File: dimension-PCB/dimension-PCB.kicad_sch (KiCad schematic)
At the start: 260 parts, among them U1 Pico, U2 Elite-Pi

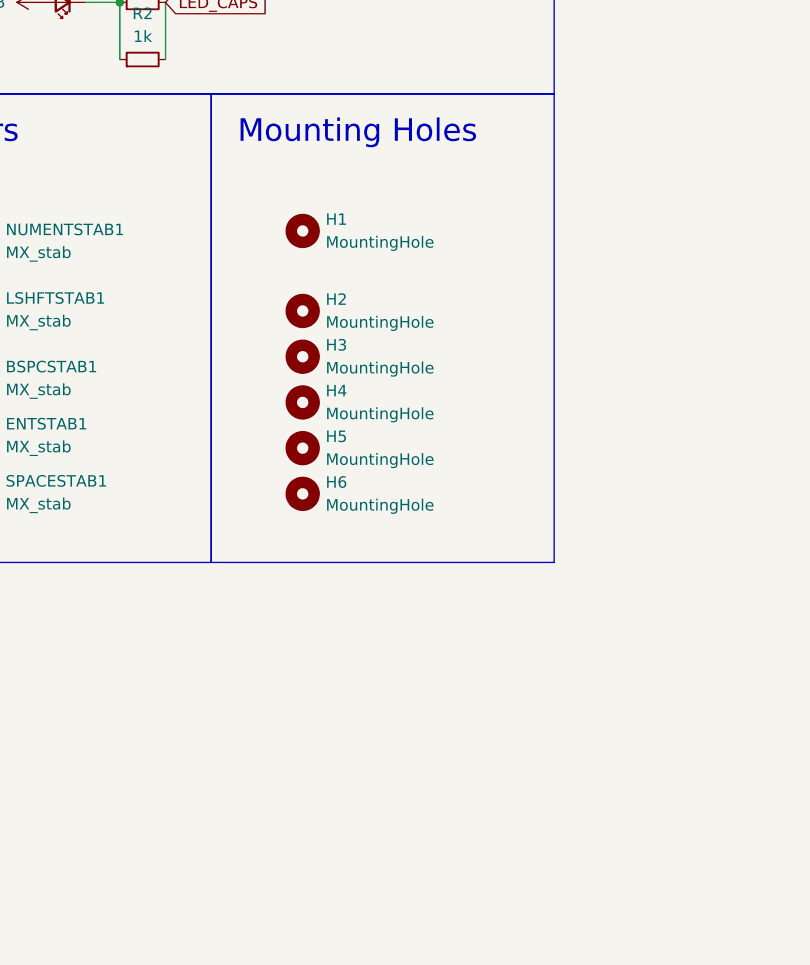
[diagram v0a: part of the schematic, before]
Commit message: Create Plate compatbility
T
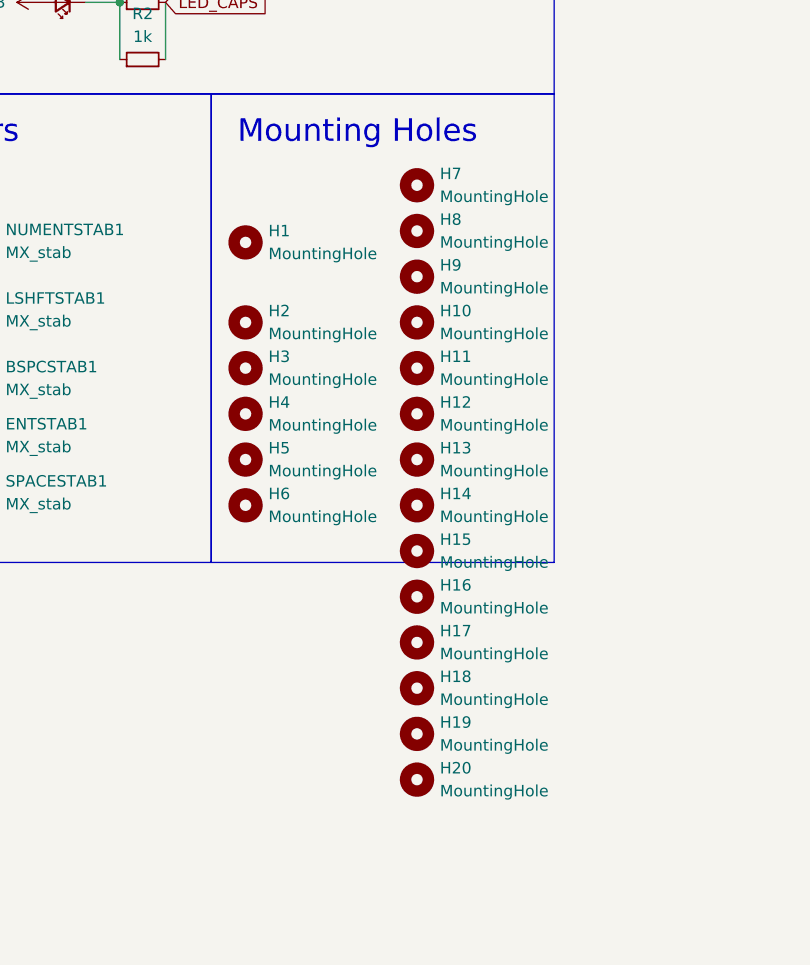
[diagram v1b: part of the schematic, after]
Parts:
- added H10, H11, H12, H13, H14, H15, H16, H17, H18, H19, H20, H7, H8, H9: MountingHole, Mount:Mount1, symbol Mechanical:MountingHole
- D118, D25, D3, D31, D34, D61, D66, D87: footprint Combo_Diode:D_SOD-123_THT_COMBO -> THTSMD_DIOD123:diode-SOD123-THT
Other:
- moved on the sheet: H1, H2, H3, H4, H5, H6
